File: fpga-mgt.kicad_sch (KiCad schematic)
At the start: 43 parts, among them U34 XCAU25P-2FFVB676I, U39 SI5319C-C-GM-ND, Y4 Resonator_114.285MHZ_ABM8

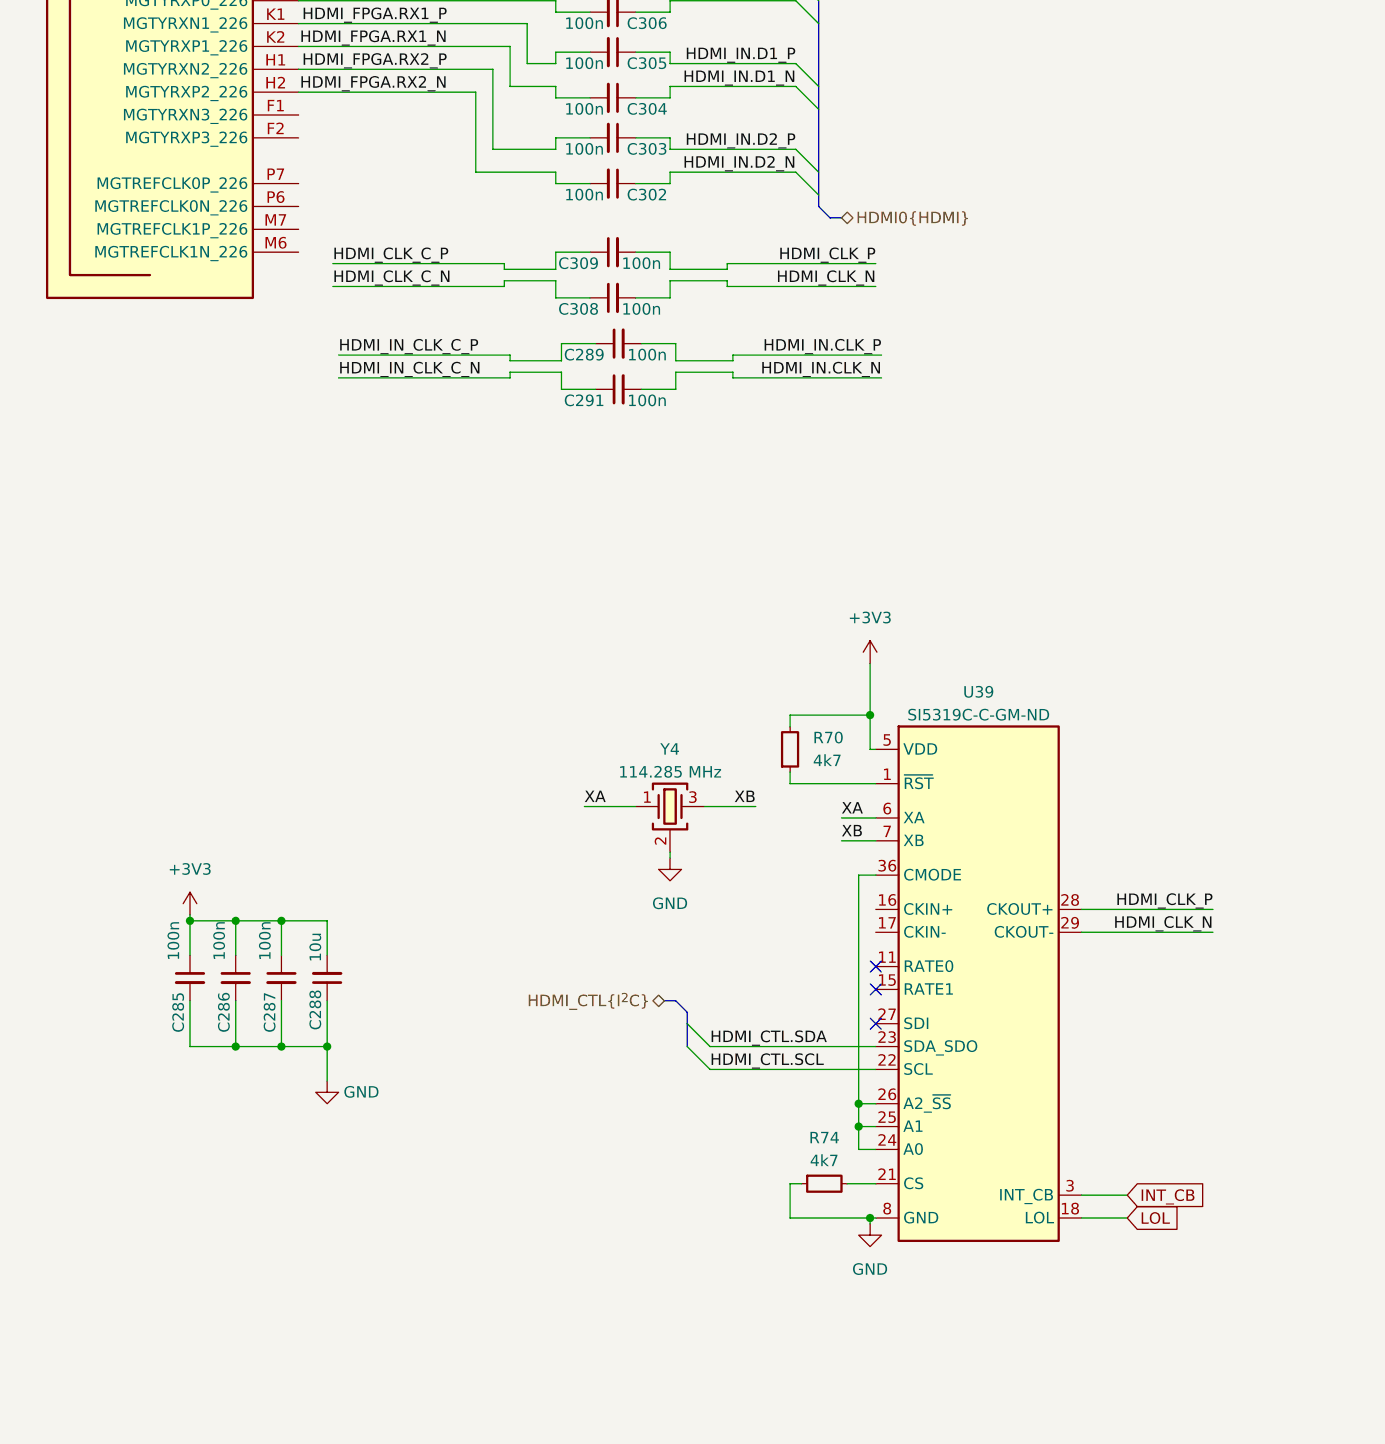
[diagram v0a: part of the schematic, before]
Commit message: [#66312] Started connecting SI5319C-C-GM-ND
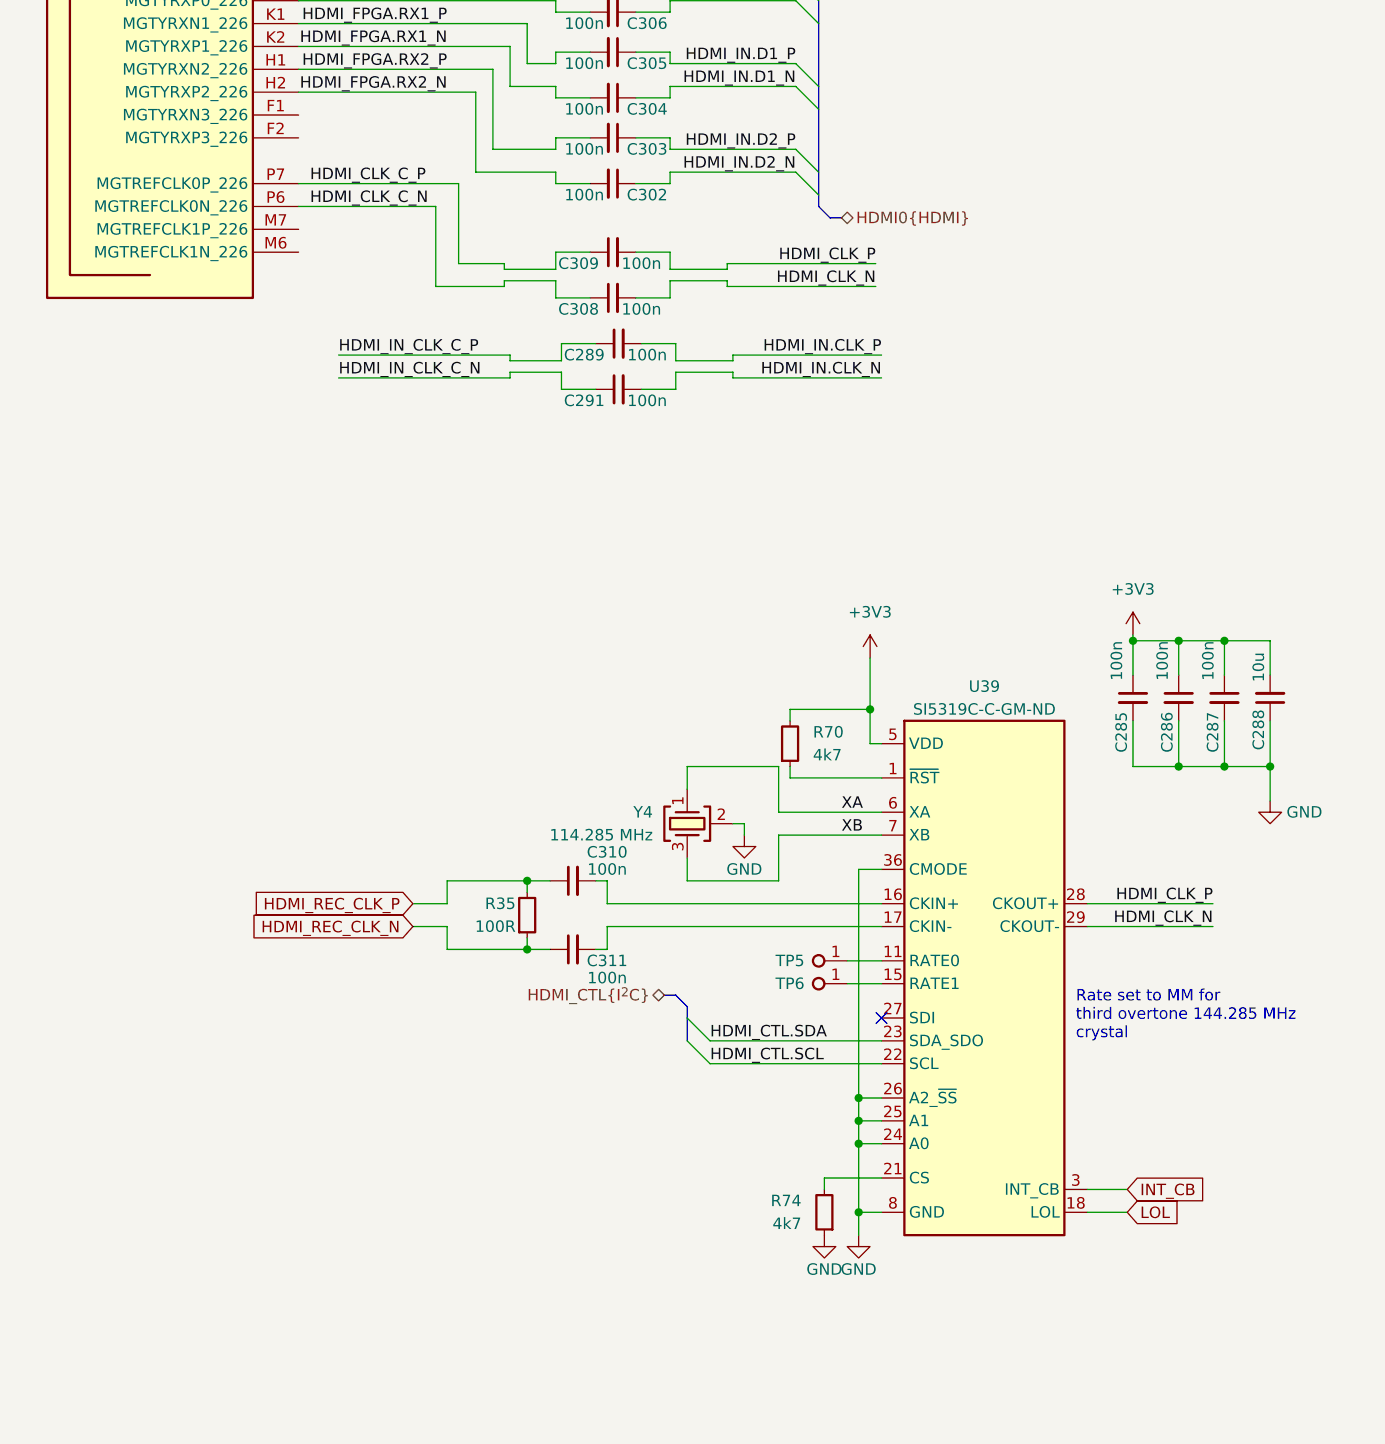
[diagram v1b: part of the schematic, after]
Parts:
- added C310, C311: C_100n_0402, antmicro-footprints:C_0402_1005Metric, symbol antmicroCapacitors0402:C_100n_0402
- added R35: R_100R_0402, antmicro-footprints:R_0402_1005Metric, symbol antmicroResistors0402:R_100R_0402
- added TP5, TP6: TP_0.75mm_SMD, antmicro-footprints:TP_SMD_0.75mm, symbol antmicroTestPoints:TP_0.75mm_SMD
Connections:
- net GND: now also U39.24 (A0), U39.25 (A1), U39.26 (A2_~{SS}), U39.36 (CMODE)
- net HDMI_CLK_C_N: now also U34.P6 (MGTREFCLK0N_226)
- net HDMI_CLK_C_P: now also U34.P7 (MGTREFCLK0P_226)
- net at U39.11 (RATE0): now also TP5.1
- net at U39.15 (RATE1): now also TP6.1
- net at U39.16 (CKIN+): now also C310.2
- net at U39.17 (CKIN-): now also C311.2
- new net HDMI_REC_CLK_N: C311.1, R35.1
- new net HDMI_REC_CLK_P: C310.1, R35.2
- no-connect marks 11 -> 9
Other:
- note added: "Rate set to MM for third overtone 144.285 MHz crystal"
- moved on the sheet: C285, C286, C287, C288, R70, R74, U39, Y4

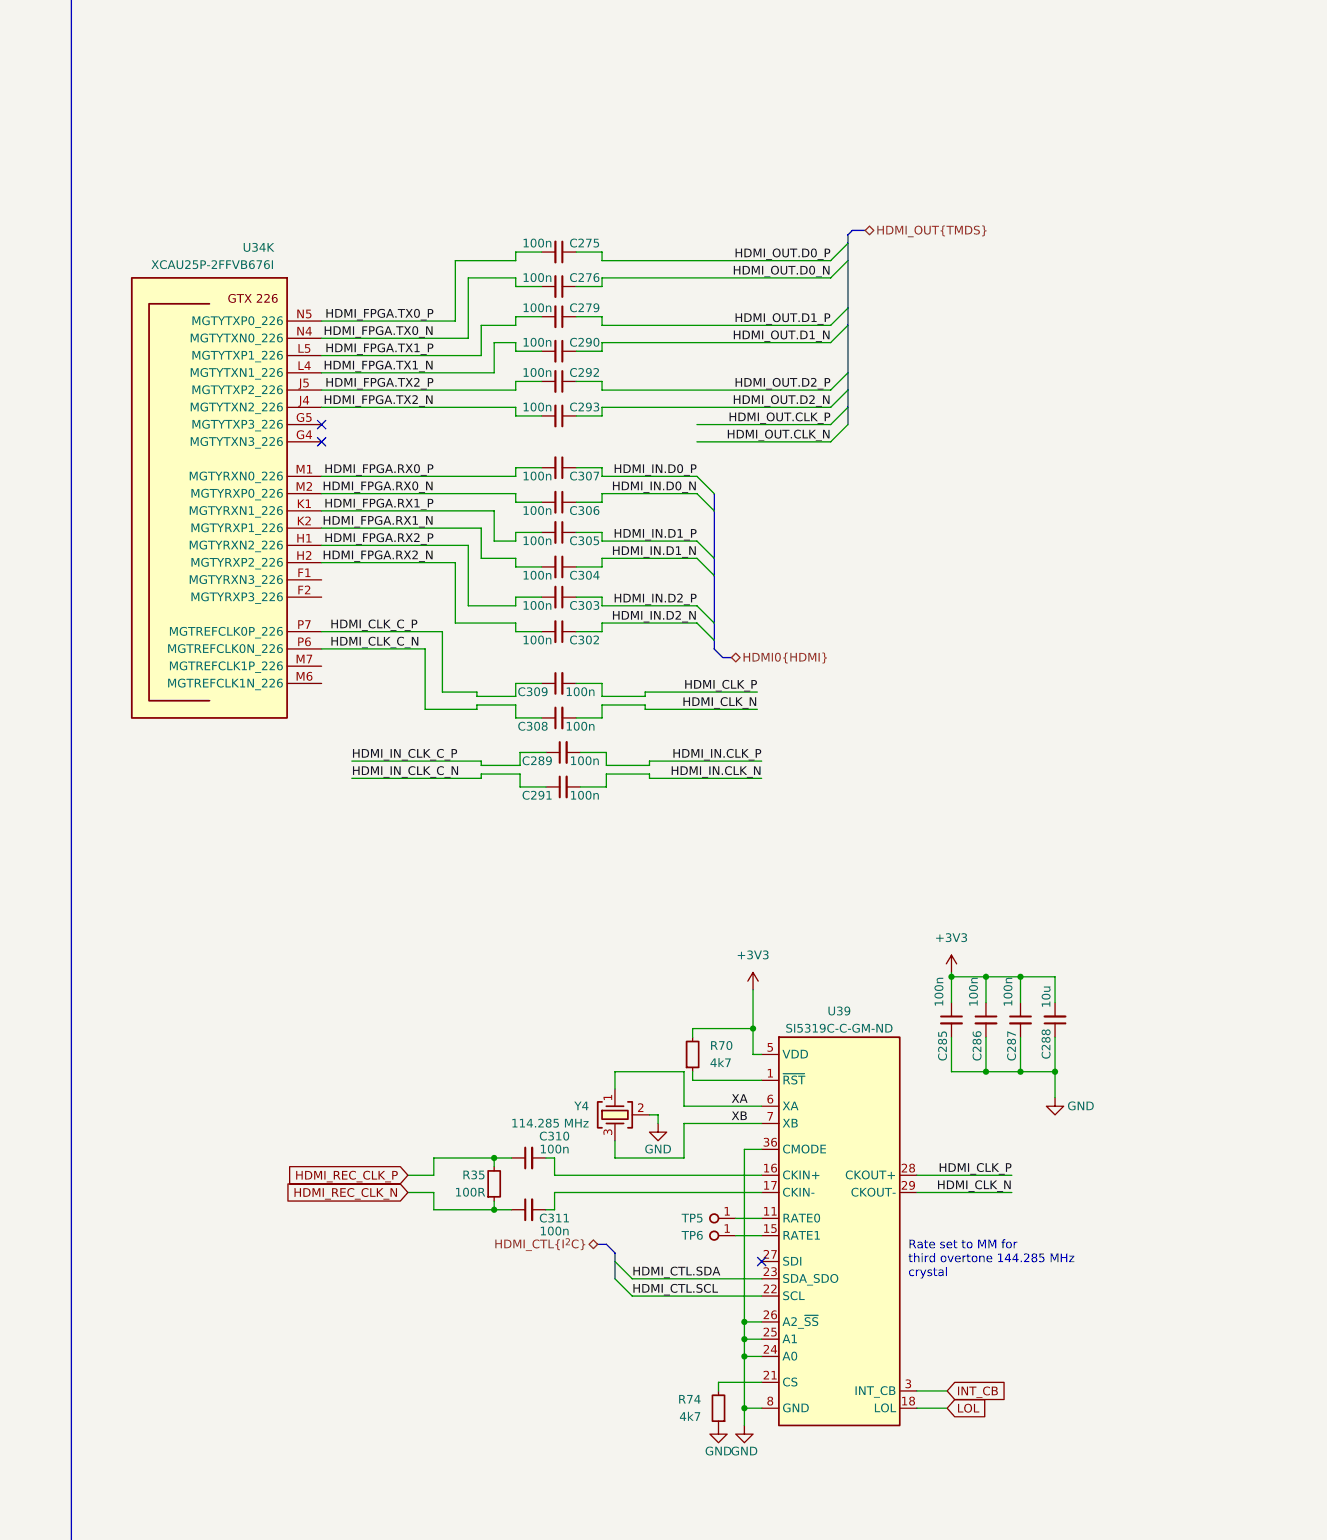
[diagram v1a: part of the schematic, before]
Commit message: [#66312] Continued HDMI schematic connections
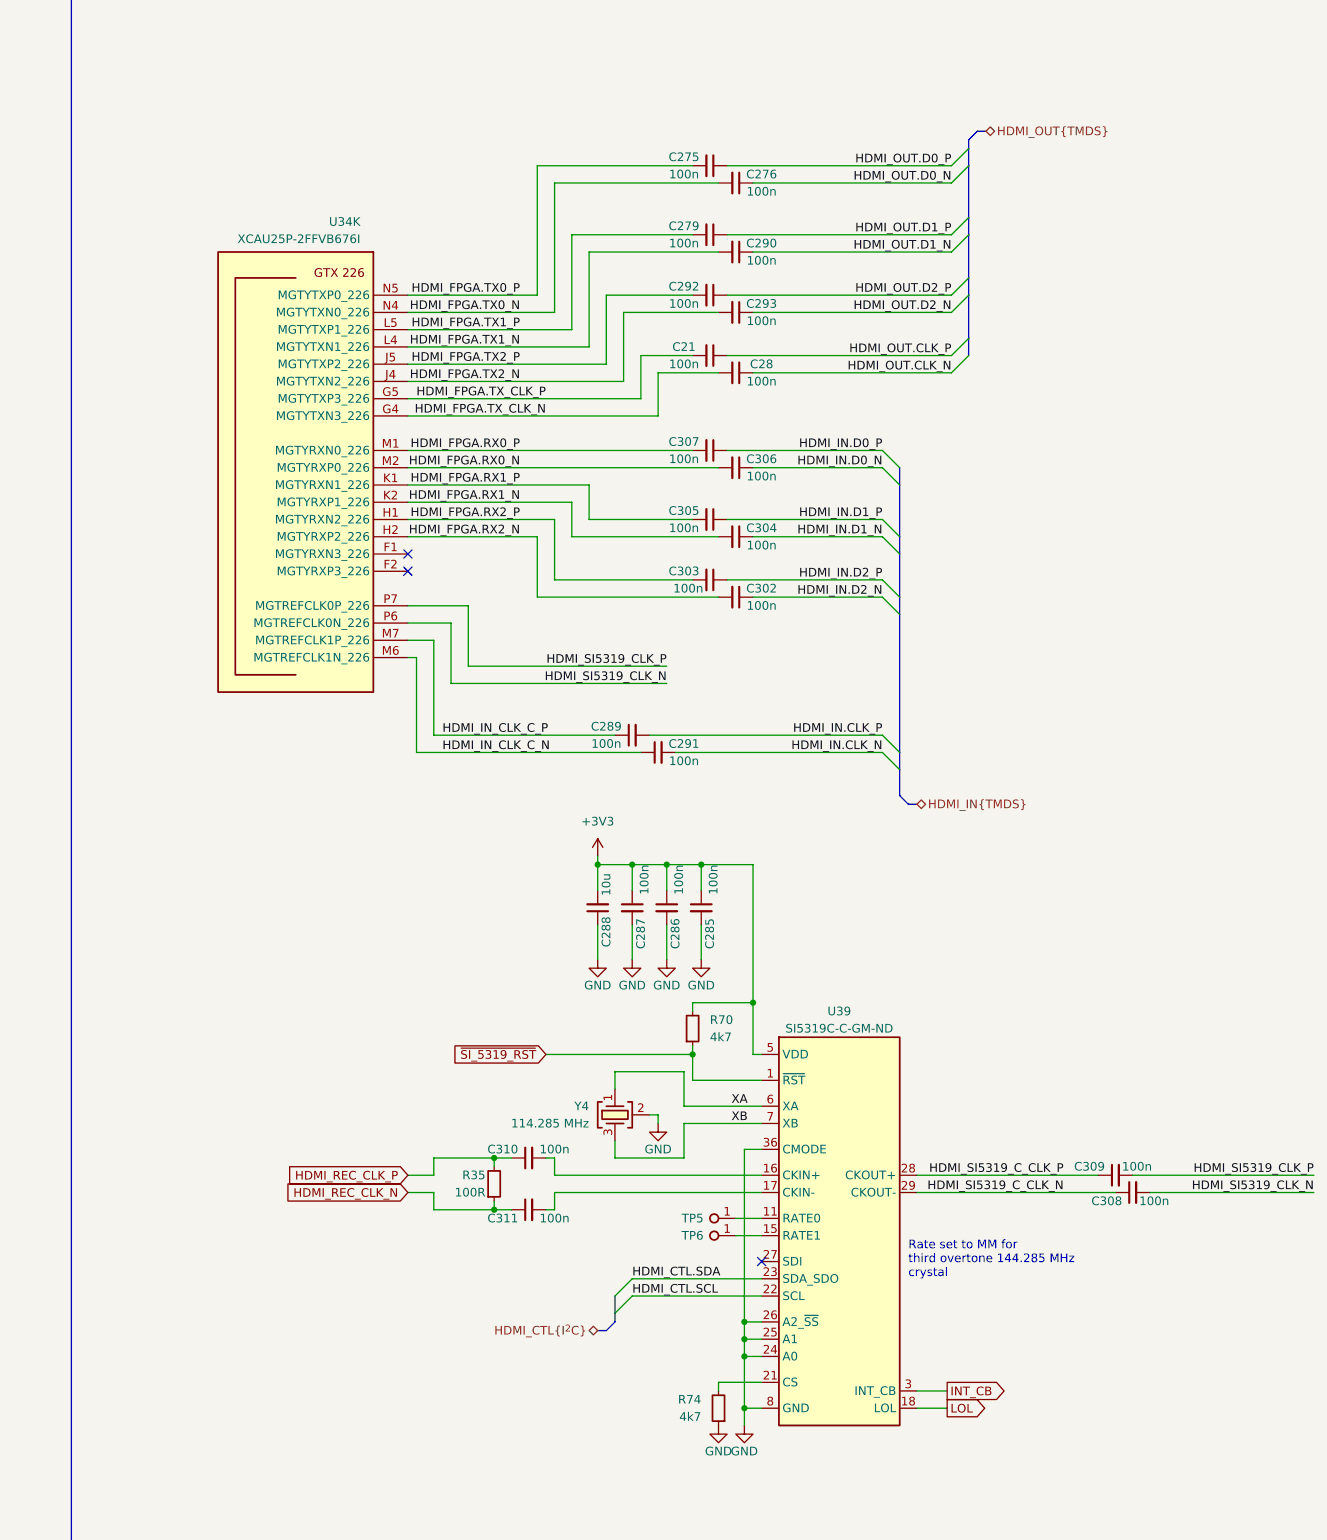
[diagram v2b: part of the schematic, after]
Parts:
- added C21, C28: C_100n_0402, antmicro-footprints:C_0402_1005Metric, symbol antmicroCapacitors0402:C_100n_0402
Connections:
- net HDMI_IN_CLK_C_N: now also U34.M6 (MGTREFCLK1N_226)
- net HDMI_IN_CLK_C_P: now also U34.M7 (MGTREFCLK1P_226)
- net HDMI_OUT.CLK_N: now also C28.1
- net HDMI_OUT.CLK_P: now also C21.1
- net HDMI_FPGA.TX_CLK_N: now reaches U34.G4 (MGTYTXN3_226)
- net HDMI_FPGA.TX_CLK_N: now also C28.2
- net HDMI_FPGA.TX_CLK_P: now reaches U34.G5 (MGTYTXP3_226)
- net HDMI_FPGA.TX_CLK_P: now also C21.2
- net ~{SI_5319_RST}: now reaches R70.1, U39.1 (~{RST})
- net HDMI_CLK_C_N renamed HDMI_SI5319_CLK_N
- net HDMI_SI5319_CLK_N: now also C308.2; no longer C308.1
- net HDMI_CLK_C_P renamed HDMI_SI5319_CLK_P
- net HDMI_SI5319_CLK_P: now also C309.2; no longer C309.1
- net HDMI_CLK_N renamed HDMI_SI5319_C_CLK_N
- net HDMI_SI5319_C_CLK_N: now also C308.1; no longer C308.2
- net HDMI_CLK_P renamed HDMI_SI5319_C_CLK_P
- net HDMI_SI5319_C_CLK_P: now also C309.1; no longer C309.2
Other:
- moved on the sheet: C275, C276, C279, C285, C286, C287, C288, C289, C290, C291, C292, C293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
